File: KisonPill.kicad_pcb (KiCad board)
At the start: 4 copper layers, 30.5 x 50 mm, 38 parts, among them J1 USB_C_Receptacle_USB2.0, J2 Conn_01x19_Male, J3 Conn_01x19_Male, Q1 2N3904S-RTK/PS, Q2 2N3904S-RTK/PS, SW1 SW_Push, SW2 SW_Push, SW3 SW_Push_DPDT, U1 CP2102N-A01-GQFN28, U2 ESP32-WROOM-32D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

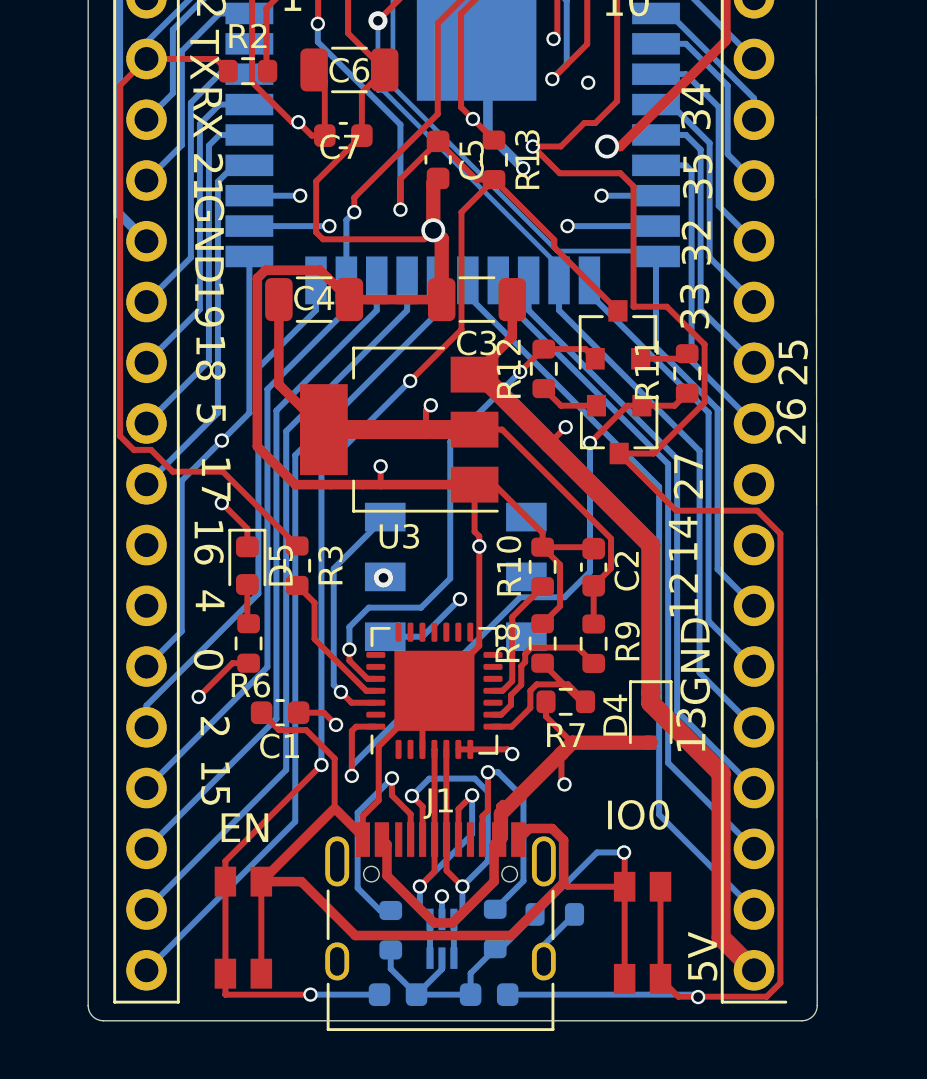
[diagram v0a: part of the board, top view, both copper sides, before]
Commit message: Modify Button
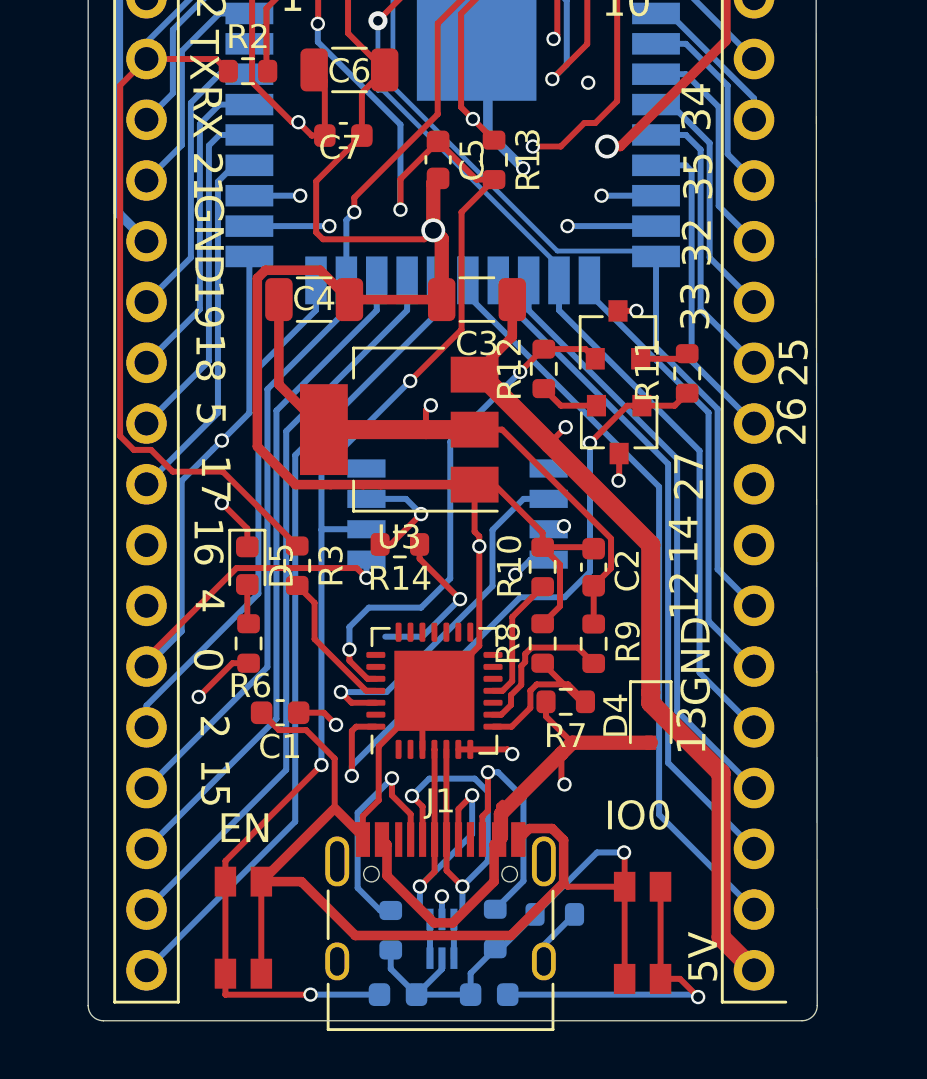
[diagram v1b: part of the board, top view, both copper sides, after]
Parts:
- added R14: 0, Resistor_SMD:R_0603_1608Metric, F.Cu at (132.2, 97.9)
- SW3: value SW_Push_DPDT -> SW_DIP_x04; footprint KisonCommon:MSS22D18G2 -> Button_Switch_SMD:SW_DIP_SPSTx04_Slide_Copal_CHS-04B_W7.62mm_P1.27mm
- moved SW3 2.54 mm to (134.6, 96.6), turned to 0 degrees
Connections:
- Q1 pad 3: /EN -> /CP2102_EN
- Q2 pad 3: /IO0 -> /CP2102_IO0
- SW3 pad 1: /CP2102TX -> /IO0
- SW3 pad 2: /ESPRX -> /EN
- SW3 pad 3: /FT2232TX -> /ESPRX
- SW3 pad 6: Net-(SW3-Pad6) -> /CP2102TX
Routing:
- net /IO0: track 129.5 -> 114.4 mm, vias 4 -> 5
- net /CP2102_EN: track 0.00 -> 11.4 mm, vias 0 -> 2
- net /CP2102_IO0: track 0.00 -> 9.01 mm, vias 0 -> 2
- net GND: track 246.8 -> 254.9 mm, vias 8 -> 7
- net /ESPRX: track 38.4 -> 45.8 mm
- net +3V3: track 135.6 -> 141.6 mm
- net /EN: track 94.8 -> 89.1 mm
- net /CP2102TX: track 10.0 -> 15.1 mm
- net /FT2232TX: track 48.9 -> 51.9 mm
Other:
- board text added: "Off-CP2102"
- board text added: "On-FT2232"
- board text removed: "CP2102"
- board text removed: "FT2232"

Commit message: V4
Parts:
- removed U4: ESP32FullConnector-KisonCommon, KisonCommon:jtag1.27-10
- C3, C4: value 22uf -> 1uf; footprint Capacitor_SMD:C_1206_3216Metric -> Capacitor_SMD:C_0603_1608Metric
- Q1, Q2: value 2N3904S-RTK/PS -> S8050
- SW3, U2: moved to F.Cu
- U3: value SPX1117M3-L-3-3/TR -> XC6206P332MR; footprint Package_TO_SOT_SMD:SOT-223-3_TabPin2 -> Package_TO_SOT_SMD:SOT-23
- U7: moved to B.Cu
- moved J2 25.4 mm to (121.6, 70.0)
- moved J3 25.4 mm to (147.0, 70.0)
- moved R2 19.8 mm to (141.1, 90.8), turned to 180 degrees
- moved C4 17.5 mm to (128.5, 105.1), turned to 90 degrees
- moved D4 17.0 mm to (125.9, 107.7), turned to 0 degrees
- moved C3 17.0 mm to (126.6, 102.2), turned to 0 degrees
- moved C6 14.4 mm to (137.0, 90.7)
- moved U3 13.4 mm to (125.9, 104.9), turned to 270 degrees
- moved R13 12.3 mm to (128.3, 91.3), turned to 180 degrees
- moved C1 12.0 mm to (139.1, 107.1)
- moved C7 10.6 mm to (131.6, 91.3)
- moved D5 9.73 mm to (129.2, 108.0), turned to 0 degrees
- moved R6 7.84 mm to (125.1, 109.9), turned to 0 degrees
- moved C5 7.74 mm to (133.0, 89.5), turned to 0 degrees
- moved R12 7.12 mm to (137.5, 97.7)
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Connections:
- U7 pad 1: /EN -> /FT2232TX
- U7 pad 10: /FT2232TX -> +3V3
- U7 pad 2: GND -> /FT2232RX
- U7 pad 3: /IO12 -> /IO0
- U7 pad 4: /IO13 -> /EN
- U7 pad 6: /IO15 -> /IO12
- U7 pad 7: +3V3 -> /IO15
- U7 pad 8: /IO0 -> /IO13
- U7 pad 9: /FT2232RX -> GND
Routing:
- net GND: track 254.9 -> 186.7 mm, vias 7 -> 9
- net +3V3: track 141.6 -> 88.3 mm, vias 6 -> 5
- net /EXT_5V: track 57.3 -> 15.2 mm, vias 2 -> 0
- net /FT2232TX: track 51.9 -> 20.6 mm
- net /IO0: track 114.4 -> 91.9 mm, vias 5 -> 3
- net /IO14: track 49.0 -> 33.4 mm, vias 3 -> 1
- net /IO12: track 48.3 -> 35.0 mm
- net /ESPRX: track 45.8 -> 34.6 mm
- net /EN: track 89.1 -> 78.7 mm, vias 5 -> 4
- net /DTR: track 27.0 -> 18.7 mm
- net /RTS: track 21.5 -> 13.4 mm
- net /IO13: track 44.9 -> 37.0 mm
- net /FT2232RX: track 25.4 -> 17.5 mm
- net /ESPTX: track 35.7 -> 42.8 mm, vias 0 -> 2
- net Net-(J1-PadB5): track 9.99 -> 3.16 mm
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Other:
- board text removed: "1"
- board text removed: "10"

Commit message: V5
Fix BJT package bug :(
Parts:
- Q1, Q2: value S8050 -> SS8050
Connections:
- Q1 pad 1: /RTS -> Net-(Q1-Pad1)
- Q1 pad 2: Net-(Q1-Pad2) -> /RTS
- Q2 pad 1: /DTR -> Net-(Q2-Pad1)
- Q2 pad 2: Net-(Q2-Pad2) -> /DTR
- R11 pad 1: Net-(Q1-Pad2) -> Net-(Q1-Pad1)
- R12 pad 1: Net-(Q2-Pad2) -> Net-(Q2-Pad1)
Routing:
- net Net-(Q1-Pad1): track 0.00 -> 4.53 mm
- net Net-(Q2-Pad1): track 0.00 -> 4.37 mm
- net /DTR: track 18.7 -> 22.9 mm
- net Net-(Q1-Pad2): track 2.65 -> 0.00 mm
- net Net-(Q2-Pad2): track 2.54 -> 0.00 mm
- net /RTS: track 13.4 -> 14.1 mm

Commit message: 封存
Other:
- board text added: "JLC Free 4-Layer NB!"
- board text added: "KisonHe KisonPillV5"
- board text removed: "KisonHe KisonPillV4"
